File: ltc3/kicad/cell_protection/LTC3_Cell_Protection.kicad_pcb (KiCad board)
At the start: 4 copper layers, 92.2 x 67.1 mm, 77 parts, among them P1 S2BPHKS, P2 PIN_HEAD_1x2, P3 MicroFit header, P4 XH header, straight, P7 MicroFit head., P8 MicroFit head., P9 XH header, straight, Q1 SUM110P08-11, Q2 SUM110P08-11, Q3 NDS9407, Q4 SUM110P08-11, Q5 SUM110P08-11, Q6 MMBT3904, U1 BQ77PL900, U2 LTC2990

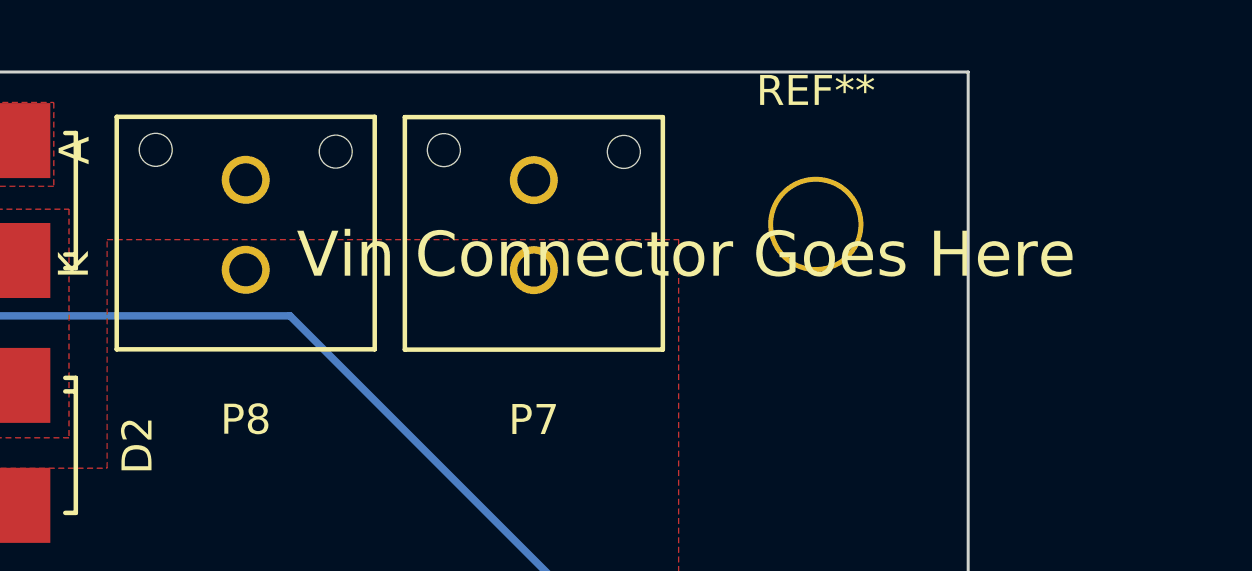
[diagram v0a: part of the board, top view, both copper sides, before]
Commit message: LTC3 Layout Work
Did a quick review and made some minor changes to layout.
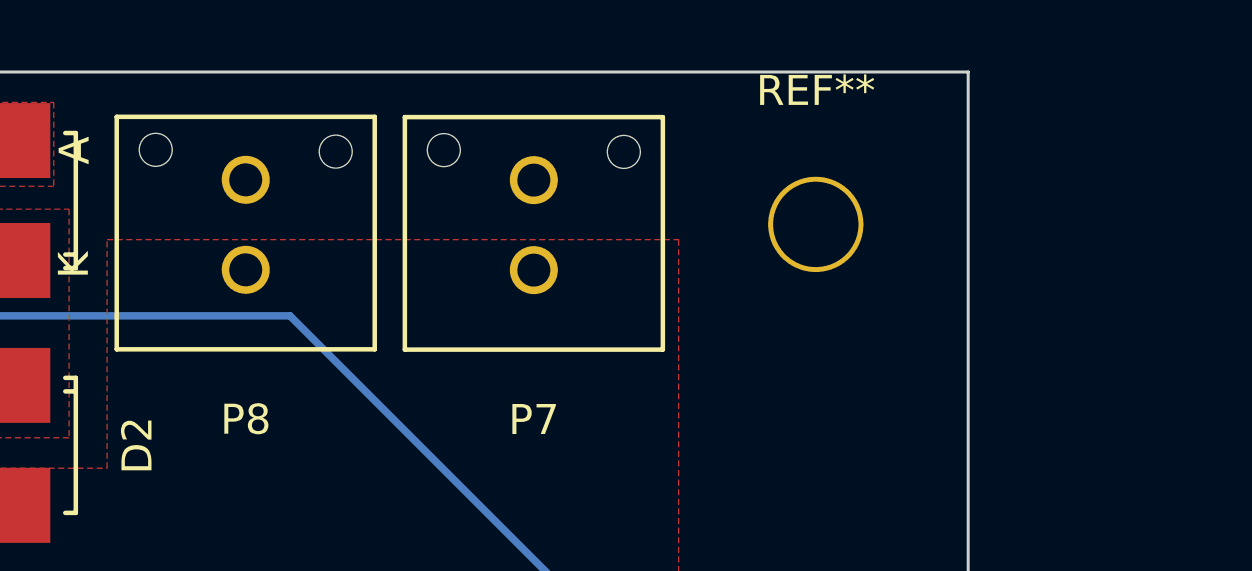
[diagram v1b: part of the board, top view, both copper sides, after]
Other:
- board text removed: "Vin Connector Goes Here"
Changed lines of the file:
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@@
     (links 155)
     (no_connects 0)
-    (area 98.441772 65.1467 201.024229 136.144001)
+    (area 98.441772 65.2608 201.024229 136.144001)
     (thickness 1.6)
-    (drawings 5)
+    (drawings 4)
     (tracks 406)
     (zones 0)
@@
     (tags "capacitor 0805")
     (attr smd)
-    (fp_text reference C19 (at -2.5273 0.1524 360) (layer F.SilkS)
+    (fp_text reference C19 (at -2.5273 0.1524) (layer F.SilkS)
       (effects (font (size 1 1) (thickness 0.15)))
     )
@@
     (tags TUMD2)
     (attr smd)
-    (fp_text reference D1 (at 2.6171 -0.127 360) (layer F.SilkS)
+    (fp_text reference D1 (at 2.6171 -0.127) (layer F.SilkS)
       (effects (font (size 1 1) (thickness 0.15)))
     )
@@
     (tags "resistor 0805")
     (attr smd)
-    (fp_text reference R22 (at -3.3147 -0.0635 360) (layer F.SilkS)
+    (fp_text reference R22 (at -3.3147 -0.0635) (layer F.SilkS)
       (effects (font (size 1 1) (thickness 0.15)))
     )
@@
     )
   )
-  (gr_text "Vin Connector Goes Here" (at 186.436 72.644) (layer F.SilkS)
-    (effects (font (size 1.5 1.5) (thickness 0.3)))
-  )
   (gr_line (start 103.632 66.548) (end 195.834 66.548) (angle 90) (layer Edge.Cuts) (width 0.1))

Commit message: LTC3: Layout Review Notes
Had a layout review this morning (hooray!) and added "TODO" notes to all
the boards and schematics.  More work to be done!
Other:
- board text added: "ground plane on each layer check to see if we can connect pin 4 to something staple around the edges and as much as we can in between"
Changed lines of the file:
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@@
     (area 98.441772 65.2608 201.024229 136.144001)
     (thickness 1.6)
-    (drawings 4)
+    (drawings 5)
     (tracks 406)
     (zones 0)
@@
     (35 F.Paste user)
     (36 B.SilkS user)
-    (37 F.SilkS user)
+    (37 F.SilkS user hide)
     (38 B.Mask user)
     (39 F.Mask user)
@@
     )
   )
+  (gr_text "ground plane on each layer\ncheck to see if we can connect pin 4 to something\nstaple around the edges and as much as we can in between" (at 155.956 50.292) (layer F.Mask)
+    (effects (font (size 1.5 1.5) (thickness 0.3)))
+  )
   (gr_line (start 103.632 66.548) (end 195.834 66.548) (angle 90) (layer Edge.Cuts) (width 0.1))

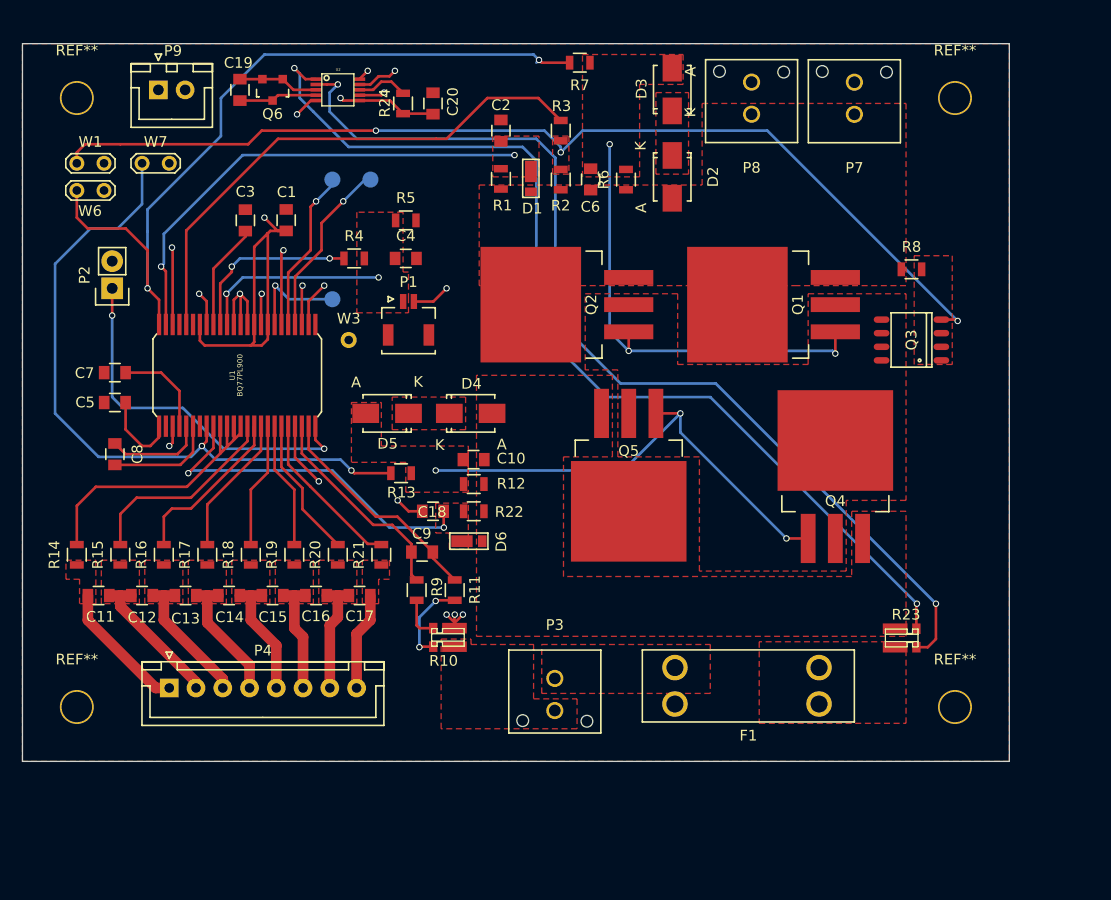
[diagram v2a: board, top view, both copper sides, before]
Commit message: LTC3 Cell Protection Layout
Reworked layout with changes to schematic and various footprints.
Also added via stapling.
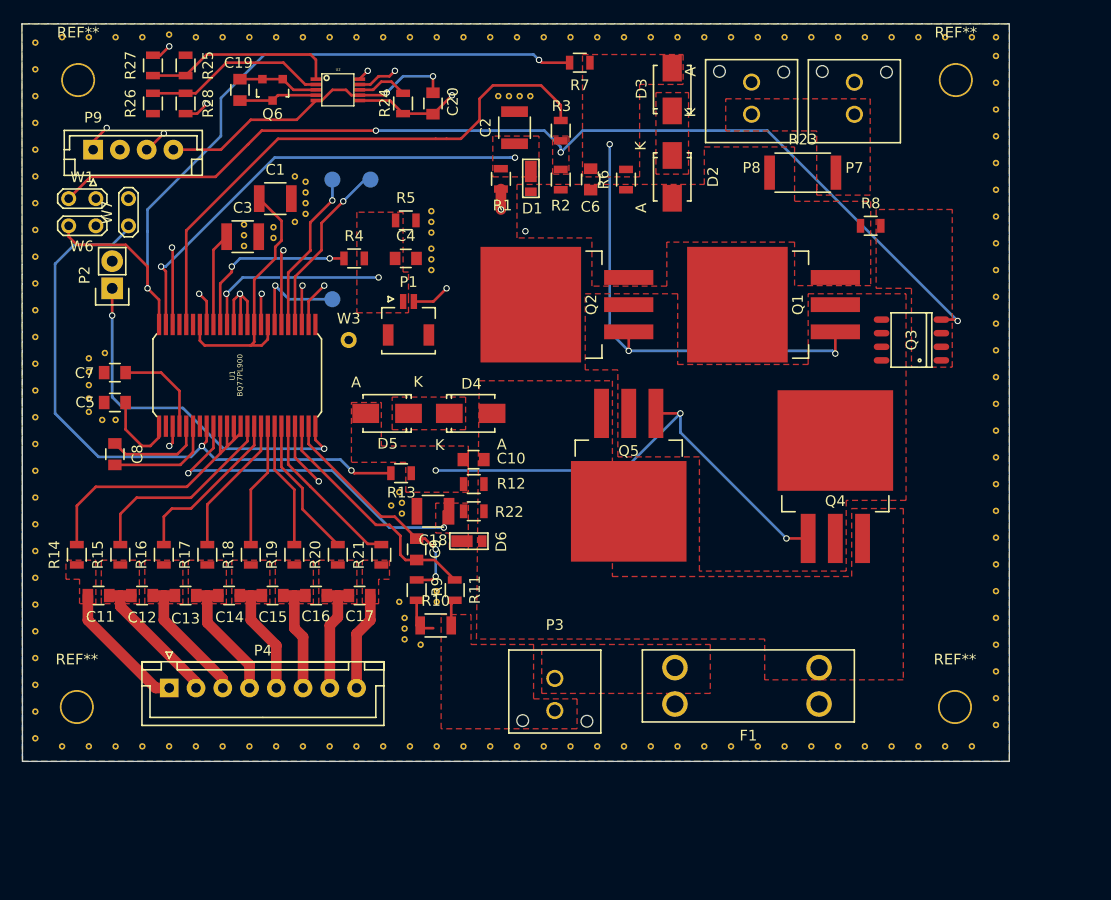
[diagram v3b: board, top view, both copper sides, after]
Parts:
- removed the REF** at (108.7, 71.6)
- removed the REF** at (190.8, 71.6)
- added R25: 12k, Resistors_SMD:R_0805, F.Cu at (118.9, 68.6)
- added R26: 12k, Resistors_SMD:R_0805, F.Cu at (115.8, 72.1)
- added R27: 75k, Resistors_SMD:R_0805, F.Cu at (115.8, 68.6)
- added R28: 75k, Resistors_SMD:R_0805, F.Cu at (118.9, 72.1)
- added REF**: Via_.6mm, LTC3:Via_.6mm, F.Cu at (111.3, 95.5)
- added REF**: Via_.6mm, LTC3:Via_.6mm, F.Cu at (141.8, 83.2)
- added REF**: Via_.6mm, LTC3:Via_.6mm, F.Cu at (194.6, 125.2)
- added REF**: Via_.6mm, LTC3:Via_.6mm, F.Cu at (194.6, 127.7)
- added REF**: Via_.6mm, LTC3:Via_.6mm, F.Cu at (194.6, 130.2)
- added REF**: Via_.6mm, LTC3:Via_.6mm, F.Cu at (192.3, 132.2)
- added REF**: Via_.6mm, LTC3:Via_.6mm, F.Cu at (189.8, 132.2)
- added REF**: Via_.6mm, LTC3:Via_.6mm, F.Cu at (187.3, 132.2)
- added REF**: Via_.6mm, LTC3:Via_.6mm, F.Cu at (184.8, 132.2)
- added REF**: Via_.6mm, LTC3:Via_.6mm, F.Cu at (182.3, 132.2)
- added REF**: Via_.6mm, LTC3:Via_.6mm, F.Cu at (179.8, 132.2)
- added REF**: Via_.6mm, LTC3:Via_.6mm, F.Cu at (177.3, 132.2)
- added REF**: Via_.6mm, LTC3:Via_.6mm, F.Cu at (141.8, 84.2)
- added REF**: Via_.6mm, LTC3:Via_.6mm, F.Cu at (174.8, 132.2)
- added REF**: Via_.6mm, LTC3:Via_.6mm, F.Cu at (172.3, 132.2)
- added REF**: Via_.6mm, LTC3:Via_.6mm, F.Cu at (169.8, 132.2)
- added REF**: Via_.6mm, LTC3:Via_.6mm, F.Cu at (167.3, 132.2)
- added REF**: Via_.6mm, LTC3:Via_.6mm, F.Cu at (164.8, 132.2)
- added REF**: Via_.6mm, LTC3:Via_.6mm, F.Cu at (162.3, 132.2)
- added REF**: Via_.6mm, LTC3:Via_.6mm, F.Cu at (159.8, 132.2)
- added REF**: Via_.6mm, LTC3:Via_.6mm, F.Cu at (157.3, 132.2)
- added REF**: Via_.6mm, LTC3:Via_.6mm, F.Cu at (154.8, 132.2)
- added REF**: Via_.6mm, LTC3:Via_.6mm, F.Cu at (152.3, 132.2)
- added REF**: Via_.6mm, LTC3:Via_.6mm, F.Cu at (141.8, 85.7)
- added REF**: Via_.6mm, LTC3:Via_.6mm, F.Cu at (149.8, 132.2)
- added REF**: Via_.6mm, LTC3:Via_.6mm, F.Cu at (147.3, 132.2)
- added REF**: Via_.6mm, LTC3:Via_.6mm, F.Cu at (144.8, 132.2)
- added REF**: Via_.6mm, LTC3:Via_.6mm, F.Cu at (142.3, 132.2)
- added REF**: Via_.6mm, LTC3:Via_.6mm, F.Cu at (139.8, 132.2)
- added REF**: Via_.6mm, LTC3:Via_.6mm, F.Cu at (137.3, 132.2)
- added REF**: Via_.6mm, LTC3:Via_.6mm, F.Cu at (134.8, 132.2)
- added REF**: Via_.6mm, LTC3:Via_.6mm, F.Cu at (132.3, 132.2)
- added REF**: Via_.6mm, LTC3:Via_.6mm, F.Cu at (129.8, 132.2)
- added REF**: Via_.6mm, LTC3:Via_.6mm, F.Cu at (127.3, 132.2)
- added REF**: Via_.6mm, LTC3:Via_.6mm, F.Cu at (141.8, 86.7)
- added REF**: Via_.6mm, LTC3:Via_.6mm, F.Cu at (124.8, 132.2)
- added REF**: Via_.6mm, LTC3:Via_.6mm, F.Cu at (122.3, 132.2)
- added REF**: Via_.6mm, LTC3:Via_.6mm, F.Cu at (119.8, 132.2)
- added REF**: Via_.6mm, LTC3:Via_.6mm, F.Cu at (117.3, 132.2)
- added REF**: Via_.6mm, LTC3:Via_.6mm, F.Cu at (114.8, 132.2)
- added REF**: Via_.6mm, LTC3:Via_.6mm, F.Cu at (112.3, 132.2)
- added REF**: Via_.6mm, LTC3:Via_.6mm, F.Cu at (109.8, 132.2)
- added REF**: Via_.6mm, LTC3:Via_.6mm, F.Cu at (107.3, 132.2)
- added REF**: Via_.6mm, LTC3:Via_.6mm, F.Cu at (104.8, 131.4)
- added REF**: Via_.6mm, LTC3:Via_.6mm, F.Cu at (104.8, 128.9)
- added REF**: Via_.6mm, LTC3:Via_.6mm, F.Cu at (141.8, 87.7)
- added REF**: Via_.6mm, LTC3:Via_.6mm, F.Cu at (104.8, 126.5)
- added REF**: Via_.6mm, LTC3:Via_.6mm, F.Cu at (104.8, 124.0)
- added REF**: Via_.6mm, LTC3:Via_.6mm, F.Cu at (104.8, 121.5)
- added REF**: Via_.6mm, LTC3:Via_.6mm, F.Cu at (104.8, 119.0)
- added REF**: Via_.6mm, LTC3:Via_.6mm, F.Cu at (104.8, 116.5)
- added REF**: Via_.6mm, LTC3:Via_.6mm, F.Cu at (104.8, 114.0)
- added REF**: Via_.6mm, LTC3:Via_.6mm, F.Cu at (104.8, 111.5)
- added REF**: Via_.6mm, LTC3:Via_.6mm, F.Cu at (104.8, 109.0)
- added REF**: Via_.6mm, LTC3:Via_.6mm, F.Cu at (104.8, 106.5)
- added REF**: Via_.6mm, LTC3:Via_.6mm, F.Cu at (104.8, 104.0)
- added REF**: Via_.6mm, LTC3:Via_.6mm, F.Cu at (138.1, 109.7)
- added REF**: Via_.6mm, LTC3:Via_.6mm, F.Cu at (104.8, 101.5)
- added REF**: Via_.6mm, LTC3:Via_.6mm, F.Cu at (104.8, 99.0)
- added REF**: Via_.6mm, LTC3:Via_.6mm, F.Cu at (104.8, 96.5)
- added REF**: Via_.6mm, LTC3:Via_.6mm, F.Cu at (104.8, 94.0)
- added REF**: Via_.6mm, LTC3:Via_.6mm, F.Cu at (104.8, 91.5)
- added REF**: Via_.6mm, LTC3:Via_.6mm, F.Cu at (104.8, 89.0)
- added REF**: Via_.6mm, LTC3:Via_.6mm, F.Cu at (104.8, 86.5)
- added REF**: Via_.6mm, LTC3:Via_.6mm, F.Cu at (104.8, 84.0)
- added REF**: Via_.6mm, LTC3:Via_.6mm, F.Cu at (104.8, 81.5)
- added REF**: Via_.6mm, LTC3:Via_.6mm, F.Cu at (104.8, 79.0)
- added REF**: Via_.6mm, LTC3:Via_.6mm, F.Cu at (139.1, 110.5)
- added REF**: Via_.6mm, LTC3:Via_.6mm, F.Cu at (104.8, 76.5)
- added REF**: Via_.6mm, LTC3:Via_.6mm, F.Cu at (104.8, 74.0)
- added REF**: Via_.6mm, LTC3:Via_.6mm, F.Cu at (104.8, 71.5)
- added REF**: Via_.6mm, LTC3:Via_.6mm, F.Cu at (104.8, 69.0)
- added REF**: MountingHole_0.1120in_#4, LTC3:MountingHole_0.1120in_number4, F.Cu at (190.8, 70.0)
- added REF**: MountingHole_0.1120in_#4, LTC3:MountingHole_0.1120in_number4, F.Cu at (108.8, 70.0)
- added REF**: Via_.6mm, LTC3:Via_.6mm, F.Cu at (104.8, 66.5)
- added REF**: Via_.6mm, LTC3:Via_.6mm, F.Cu at (139.1, 109.5)
- added REF**: Via_.6mm, LTC3:Via_.6mm, F.Cu at (138.8, 108.5)
- added REF**: Via_.6mm, LTC3:Via_.6mm, F.Cu at (142.3, 117.7)
- added REF**: Via_.6mm, LTC3:Via_.6mm, F.Cu at (112.3, 101.7)
- added REF**: Via_.6mm, LTC3:Via_.6mm, F.Cu at (142.3, 118.7)
- added REF**: Via_.6mm, LTC3:Via_.6mm, F.Cu at (138.8, 118.7)
- added REF**: Via_.6mm, LTC3:Via_.6mm, F.Cu at (139.3, 120.2)
- added REF**: Via_.6mm, LTC3:Via_.6mm, F.Cu at (139.3, 121.2)
- added REF**: Via_.6mm, LTC3:Via_.6mm, F.Cu at (139.3, 122.2)
- added REF**: Via_.6mm, LTC3:Via_.6mm, F.Cu at (140.8, 122.7)
- added REF**: Via_.6mm, LTC3:Via_.6mm, F.Cu at (148.1, 71.5)
- added REF**: Via_.6mm, LTC3:Via_.6mm, F.Cu at (149.1, 71.5)
- added REF**: Via_.6mm, LTC3:Via_.6mm, F.Cu at (150.1, 71.5)
- added REF**: Via_.6mm, LTC3:Via_.6mm, F.Cu at (151.1, 71.5)
- added REF**: Via_.6mm, LTC3:Via_.6mm, F.Cu at (109.8, 101.0)
- added REF**: Via_.6mm, LTC3:Via_.6mm, F.Cu at (124.3, 83.5)
- added REF**: Via_.6mm, LTC3:Via_.6mm, F.Cu at (130.1, 79.5)
- added REF**: Via_.6mm, LTC3:Via_.6mm, F.Cu at (127.1, 84.7)
- added REF**: Via_.6mm, LTC3:Via_.6mm, F.Cu at (124.3, 84.5)
- added REF**: Via_.6mm, LTC3:Via_.6mm, F.Cu at (124.3, 85.5)
- added REF**: Via_.6mm, LTC3:Via_.6mm, F.Cu at (127.1, 83.7)
- added REF**: Via_.6mm, LTC3:Via_.6mm, F.Cu at (129.1, 79.0)
- added REF**: Via_.6mm, LTC3:Via_.6mm, F.Cu at (129.1, 83.2)
- added REF**: Via_.6mm, LTC3:Via_.6mm, F.Cu at (130.1, 82.5)
- added REF**: Via_.6mm, LTC3:Via_.6mm, F.Cu at (130.1, 81.5)
- added REF**: Via_.6mm, LTC3:Via_.6mm, F.Cu at (111.1, 101.7)
- added REF**: Via_.6mm, LTC3:Via_.6mm, F.Cu at (130.1, 80.5)
- added REF**: Via_.6mm, LTC3:Via_.6mm, F.Cu at (117.3, 65.7)
- added REF**: Via_.6mm, LTC3:Via_.6mm, F.Cu at (194.6, 66.0)
- added REF**: Via_.6mm, LTC3:Via_.6mm, F.Cu at (192.3, 66.0)
- added REF**: Via_.6mm, LTC3:Via_.6mm, F.Cu at (189.8, 66.0)
- added REF**: Via_.6mm, LTC3:Via_.6mm, F.Cu at (187.3, 66.0)
- added REF**: Via_.6mm, LTC3:Via_.6mm, F.Cu at (184.8, 66.0)
- added REF**: Via_.6mm, LTC3:Via_.6mm, F.Cu at (182.3, 66.0)
- added REF**: Via_.6mm, LTC3:Via_.6mm, F.Cu at (179.8, 66.0)
- added REF**: Via_.6mm, LTC3:Via_.6mm, F.Cu at (177.3, 66.0)
- added REF**: Via_.6mm, LTC3:Via_.6mm, F.Cu at (109.8, 99.7)
- added REF**: Via_.6mm, LTC3:Via_.6mm, F.Cu at (174.8, 66.0)
- added REF**: Via_.6mm, LTC3:Via_.6mm, F.Cu at (172.3, 66.0)
- added REF**: Via_.6mm, LTC3:Via_.6mm, F.Cu at (169.8, 66.0)
- added REF**: Via_.6mm, LTC3:Via_.6mm, F.Cu at (167.3, 66.0)
- added REF**: Via_.6mm, LTC3:Via_.6mm, F.Cu at (164.8, 66.0)
- added REF**: Via_.6mm, LTC3:Via_.6mm, F.Cu at (162.3, 66.0)
- added REF**: Via_.6mm, LTC3:Via_.6mm, F.Cu at (159.8, 66.0)
- added REF**: Via_.6mm, LTC3:Via_.6mm, F.Cu at (157.3, 66.0)
- added REF**: Via_.6mm, LTC3:Via_.6mm, F.Cu at (154.8, 66.0)
- added REF**: Via_.6mm, LTC3:Via_.6mm, F.Cu at (152.3, 66.0)
- added REF**: Via_.6mm, LTC3:Via_.6mm, F.Cu at (109.8, 98.5)
- added REF**: Via_.6mm, LTC3:Via_.6mm, F.Cu at (149.8, 66.0)
- added REF**: Via_.6mm, LTC3:Via_.6mm, F.Cu at (147.3, 66.0)
- added REF**: Via_.6mm, LTC3:Via_.6mm, F.Cu at (144.8, 66.0)
- added REF**: Via_.6mm, LTC3:Via_.6mm, F.Cu at (142.3, 66.0)
- added REF**: Via_.6mm, LTC3:Via_.6mm, F.Cu at (139.8, 66.0)
- added REF**: Via_.6mm, LTC3:Via_.6mm, F.Cu at (137.3, 66.0)
- added REF**: Via_.6mm, LTC3:Via_.6mm, F.Cu at (134.8, 66.0)
- added REF**: Via_.6mm, LTC3:Via_.6mm, F.Cu at (132.3, 66.0)
- added REF**: Via_.6mm, LTC3:Via_.6mm, F.Cu at (129.8, 66.0)
- added REF**: Via_.6mm, LTC3:Via_.6mm, F.Cu at (127.3, 66.0)
- added REF**: Via_.6mm, LTC3:Via_.6mm, F.Cu at (109.8, 97.2)
- added REF**: Via_.6mm, LTC3:Via_.6mm, F.Cu at (124.8, 66.0)
- added REF**: Via_.6mm, LTC3:Via_.6mm, F.Cu at (122.3, 66.0)
- added REF**: Via_.6mm, LTC3:Via_.6mm, F.Cu at (119.8, 66.0)
- added REF**: Via_.6mm, LTC3:Via_.6mm, F.Cu at (114.8, 66.0)
- added REF**: Via_.6mm, LTC3:Via_.6mm, F.Cu at (112.3, 66.0)
- added REF**: Via_.6mm, LTC3:Via_.6mm, F.Cu at (109.8, 66.0)
- added REF**: Via_.6mm, LTC3:Via_.6mm, F.Cu at (107.3, 66.0)
- added REF**: Via_.6mm, LTC3:Via_.6mm, F.Cu at (194.6, 67.7)
- added REF**: Via_.6mm, LTC3:Via_.6mm, F.Cu at (194.6, 70.2)
- added REF**: Via_.6mm, LTC3:Via_.6mm, F.Cu at (194.6, 72.7)
- added REF**: Via_.6mm, LTC3:Via_.6mm, F.Cu at (109.8, 96.0)
- added REF**: Via_.6mm, LTC3:Via_.6mm, F.Cu at (194.6, 75.2)
- added REF**: Via_.6mm, LTC3:Via_.6mm, F.Cu at (194.6, 77.7)
- added REF**: Via_.6mm, LTC3:Via_.6mm, F.Cu at (194.6, 80.2)
- added REF**: Via_.6mm, LTC3:Via_.6mm, F.Cu at (194.6, 82.7)
- added REF**: Via_.6mm, LTC3:Via_.6mm, F.Cu at (194.6, 85.2)
- added REF**: Via_.6mm, LTC3:Via_.6mm, F.Cu at (194.6, 87.7)
- added REF**: Via_.6mm, LTC3:Via_.6mm, F.Cu at (194.6, 90.2)
- added REF**: Via_.6mm, LTC3:Via_.6mm, F.Cu at (194.6, 92.7)
- added REF**: Via_.6mm, LTC3:Via_.6mm, F.Cu at (194.6, 95.2)
- added REF**: Via_.6mm, LTC3:Via_.6mm, F.Cu at (194.6, 97.7)
- added REF**: Via_.6mm, LTC3:Via_.6mm, F.Cu at (141.8, 82.2)
- added REF**: Via_.6mm, LTC3:Via_.6mm, F.Cu at (194.6, 100.2)
- added REF**: Via_.6mm, LTC3:Via_.6mm, F.Cu at (194.6, 102.7)
- added REF**: Via_.6mm, LTC3:Via_.6mm, F.Cu at (194.6, 105.2)
- added REF**: Via_.6mm, LTC3:Via_.6mm, F.Cu at (194.6, 107.7)
- added REF**: Via_.6mm, LTC3:Via_.6mm, F.Cu at (194.6, 110.2)
- added REF**: Via_.6mm, LTC3:Via_.6mm, F.Cu at (194.6, 112.7)
- added REF**: Via_.6mm, LTC3:Via_.6mm, F.Cu at (194.6, 115.2)
- added REF**: Via_.6mm, LTC3:Via_.6mm, F.Cu at (194.6, 117.7)
- added REF**: Via_.6mm, LTC3:Via_.6mm, F.Cu at (194.6, 120.2)
- added REF**: Via_.6mm, LTC3:Via_.6mm, F.Cu at (194.6, 122.7)
- C1, C18, C2, C3: footprint Capacitors_SMD:C_0805 -> Capacitors_SMD:C_1210
- P1: value S2BPHKS -> XH header
- P4: value XH header, straight -> XH header
- P7, P8: value MicroFit head. -> MicroFit header
- P9: value XH header, straight -> XH header; footprint Connectors_JST:JST_XH_B02B-XH-A_02x2.50mm_Straight -> Connectors_JST:JST_EH_B04B-EH-A_04x2.50mm_Straight
- R10: footprint LTC3:CST0612 -> Resistors_SMD:R_1206
- R14, R15, R16, R17, R18, R19, R20, R21: value 500 -> 510
- R23: value 30m -> 60m; footprint LTC3:CST0612 -> Resistors_SMD:R_2512
- moved R23 45.2 mm to (176.5, 78.6)
- moved P9 8.27 mm to (110.2, 76.5)
- moved W7 5.98 mm to (113.5, 83.6), turned to 90 degrees
- moved R8 5.57 mm to (182.9, 83.6)
- moved W6 3.39 mm to (108.0, 83.6)
- moved W1 3.39 mm to (108.0, 81.0)
- moved C1 2.26 mm to (127.3, 81.0), turned to 0 degrees
- moved R10 1.80 mm to (142.2, 120.9), turned to 0 degrees
- moved C3 1.55 mm to (124.2, 84.6), turned to 0 degrees
- moved C2 1.30 mm to (149.6, 74.4)
- moved C9 0.57 mm to (140.5, 113.8), turned to 270 degrees
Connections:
- C1 pad 1: +5V -> Net-(C1-Pad1)
- C20 pad 2: GND -> GNDREF
- C6 pad 1: /VBATT -> Net-(C6-Pad1)
- D1 pad 2: /VBATT -> Net-(C6-Pad1)
- D2 pad 2: /VBATT -> Net-(C6-Pad1)
- F1 pad 1: Net-(F1-Pad1) -> Net-(C10-Pad1)
- P9 pad 1: /I2C_DATA -> +5V
- Q1 pad 3: /VBATT -> Net-(C6-Pad1)
- Q2 pad 3: /VBATT -> Net-(C6-Pad1)
- Q3 pad 1: Net-(Q3-Pad1) -> (no net)
- Q3 pad 2: Net-(Q3-Pad1) -> (no net)
- Q3 pad 3: Net-(Q3-Pad1) -> Net-(Q3-Pad3)
- Q3 pad 6: Net-(Q1-Pad2) -> (no net)
- Q3 pad 7: Net-(Q1-Pad2) -> (no net)
- Q3 pad 8: Net-(Q1-Pad2) -> (no net)
- R11 pad 2: Net-(R10-Pad4) -> Net-(P3-Pad2)
- R2 pad 1: /VBATT -> Net-(C6-Pad1)
- R23 pad 1: Net-(F1-Pad1) -> Net-(C6-Pad1)
- R23 pad 2: Net-(C10-Pad1) -> /VBATT
- R6 pad 1: /VBATT -> Net-(C6-Pad1)
- R8 pad 1: /VBATT -> Net-(C6-Pad1)
- R8 pad 2: Net-(Q3-Pad1) -> Net-(Q3-Pad3)
- R9 pad 2: Net-(R10-Pad3) -> GND
- U1 pad 22: Net-(C9-Pad1) -> Net-(C9-Pad2)
- U1 pad 23: Net-(C9-Pad2) -> Net-(C9-Pad1)
- U1 pad 32: +5V -> Net-(C1-Pad1)
- U1 pad 34: +5V -> Net-(C1-Pad1)
- U1 pad 42: +5V -> Net-(C1-Pad1)
- U2 pad 1: Net-(R23-Pad4) -> Net-(R25-Pad2)
- U2 pad 2: Net-(R23-Pad3) -> Net-(R26-Pad2)
- U2 pad 3: Net-(C19-Pad1) -> (no net)
- U2 pad 4: Net-(C19-Pad2) -> (no net)
- U2 pad 5: GND -> GNDREF
- U2 pad 9: GND -> GNDREF
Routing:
- net Net-(R23-Pad3): track 94.8 -> 0.00 mm, vias 2 -> 0
- net Net-(R23-Pad4): track 94.1 -> 0.00 mm, vias 2 -> 0
- net /VBATT: track 0.00 -> 75.9 mm, vias 0 -> 2
- net Net-(C6-Pad1): track 0.00 -> 47.5 mm, vias 0 -> 2
- net GNDREF: track 0.00 -> 29.0 mm, vias 0 -> 2
- net Net-(C1-Pad1): track 0.00 -> 25.5 mm
- net Net-(R25-Pad2): track 0.00 -> 18.1 mm
- net Net-(R26-Pad2): track 0.00 -> 17.4 mm
- net /I2C_CLK: track 45.1 -> 54.8 mm
- net +5V: track 57.3 -> 48.9 mm
- net Net-(R10-Pad4): track 8.07 -> 0.00 mm, vias 2 -> 0
- net GND: track 52.9 -> 45.1 mm, vias 14 -> 8
- net Net-(R13-Pad2): track 64.8 -> 59.0 mm
- net (no net): track 0.00 -> 4.06 mm
- net Net-(R10-Pad3): track 4.01 -> 0.00 mm
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- added copper zone on B.Cu, net GND
- added copper zone on In2.Cu, net GND
- added copper zone on F.Cu, net Net-(C6-Pad1)
- added copper zone on F.Cu, net Net-(Q3-Pad3)
- removed copper zone on F.Cu, net Net-(F1-Pad1)
- removed copper zone on F.Cu, net Net-(Q3-Pad1)
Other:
- board size 92.2 x 67.1 mm -> 92.2 x 68.9 mm
- board text removed: "ground plane on each layer check to see if we can connect pin 4 to something staple around the edges and as much as we can in between"

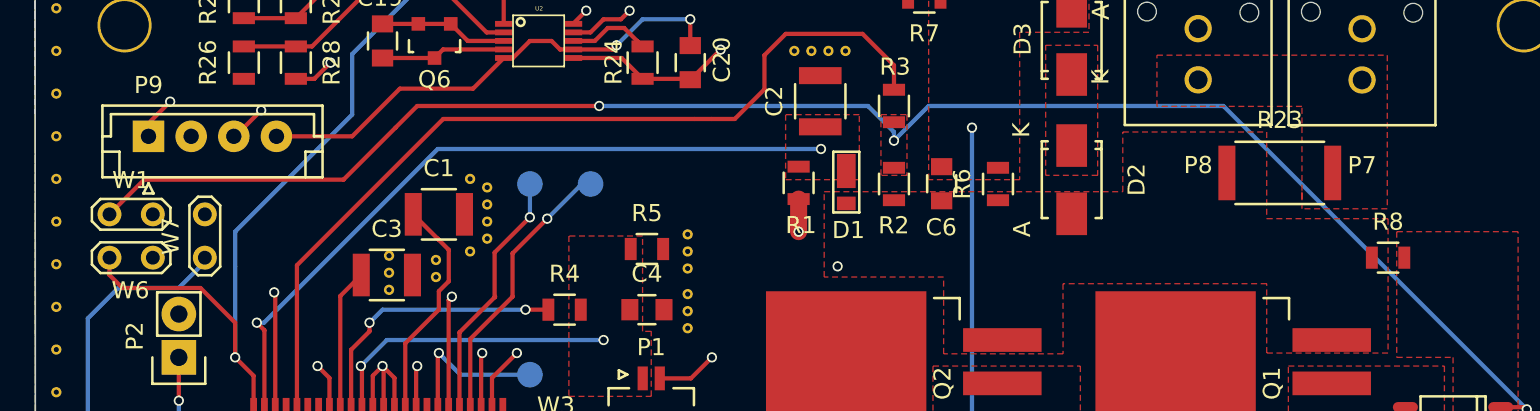
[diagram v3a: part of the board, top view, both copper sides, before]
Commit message: LTC3 Cell Protection Layout
A little bit of work on the silk screen for the board layout.
We moved the temp sensing to off board, do we still want footprints for
these on the cell protection board?
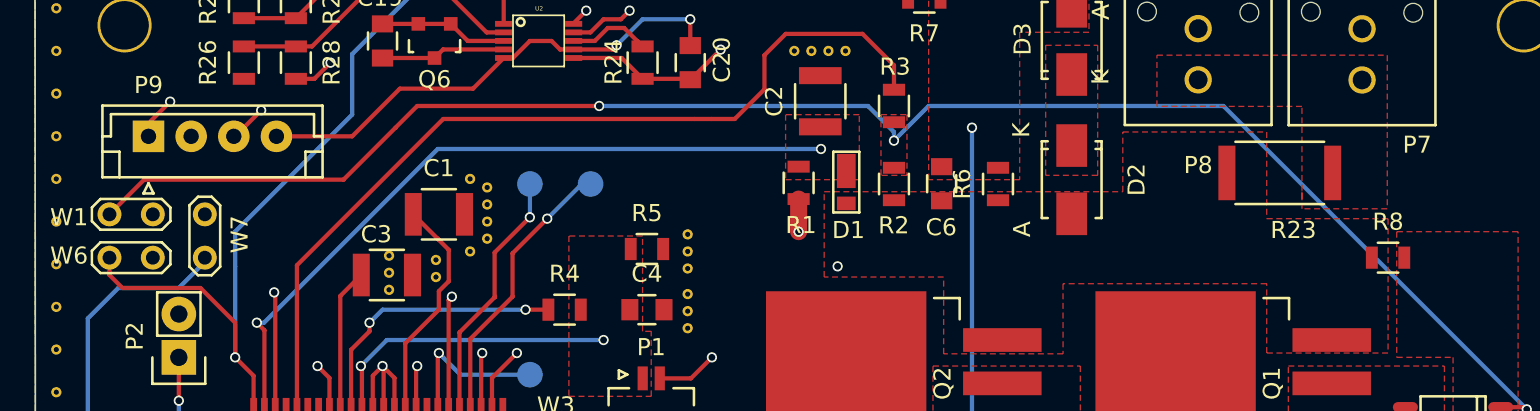
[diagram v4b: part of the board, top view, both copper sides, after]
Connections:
- Q3 pad 1: (no net) -> Net-(Q3-Pad1)
- Q3 pad 2: (no net) -> Net-(Q3-Pad1)
- Q3 pad 3: Net-(Q3-Pad3) -> Net-(Q3-Pad1)
- Q3 pad 6: (no net) -> Net-(Q1-Pad2)
- Q3 pad 7: (no net) -> Net-(Q1-Pad2)
- Q3 pad 8: (no net) -> Net-(Q1-Pad2)
- R8 pad 2: Net-(Q3-Pad3) -> Net-(Q3-Pad1)
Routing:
- added copper zone on F.Cu, net Net-(Q3-Pad1)
- removed copper zone on F.Cu, net Net-(Q3-Pad3)
